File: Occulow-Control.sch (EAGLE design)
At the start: 39 parts, among them J1 CORTEX_DEBUG_PTH, T1 DMP3010LK3, T2 DMP3010LK3, T3 DMP3010LK3

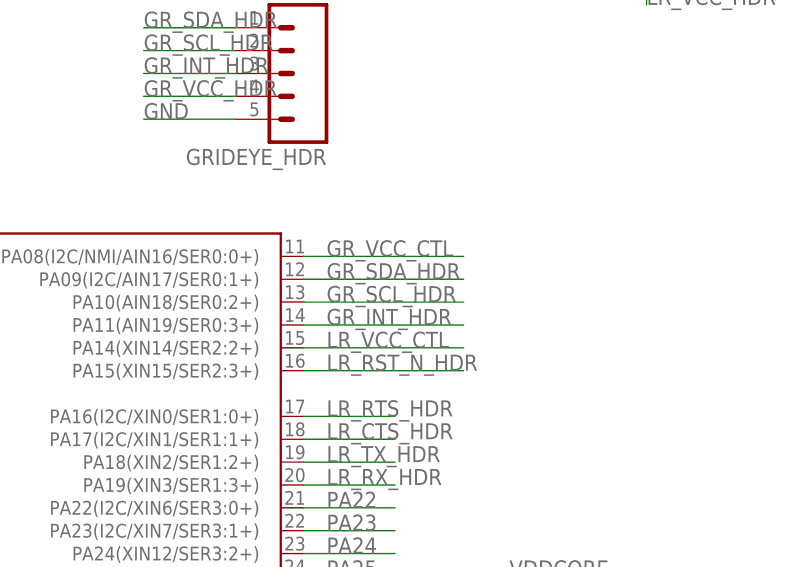
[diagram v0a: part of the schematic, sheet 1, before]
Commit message: Move schematic grideye pins to i2c pads, fixes #2
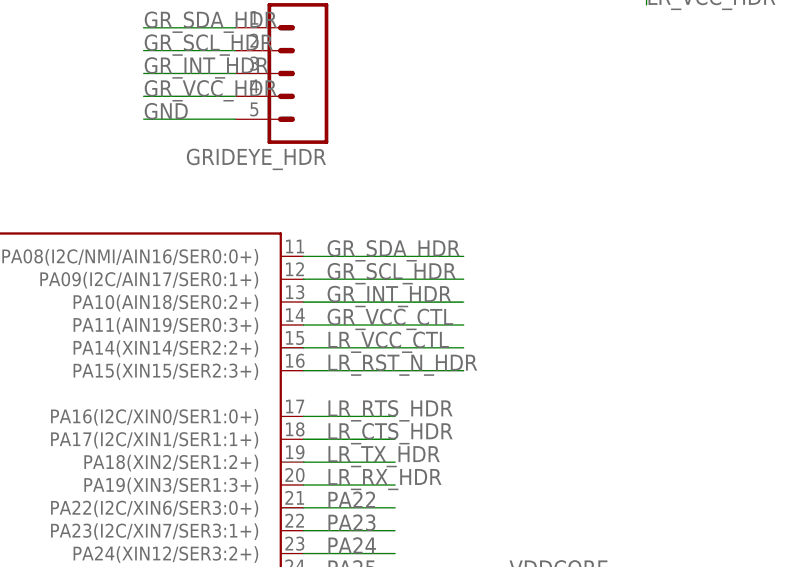
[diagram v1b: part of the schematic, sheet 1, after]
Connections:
- net GR_INT_HDR: now also U$1.PA10(AIN18/SER0:2+); no longer U$1.PA11(AIN19/SER0:3+)
- net GR_SCL_HDR: now also U$1.PA09(I2C/AIN17/SER0:1+); no longer U$1.PA10(AIN18/SER0:2+)
- net GR_SDA_HDR: now also U$1.PA08(I2C/NMI/AIN16/SER0:0+); no longer U$1.PA09(I2C/AIN17/SER0:1+)
- net GR_VCC_CTL: now also U$1.PA11(AIN19/SER0:3+); no longer U$1.PA08(I2C/NMI/AIN16/SER0:0+)
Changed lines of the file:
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@@
 </segment>
 <segment>
-<pinref part="U$1" gate="G$1" pin="PA09(I2C/AIN17/SER0:1+)"/>
-<wire x1="142.24" y1="93.98" x2="160.02" y2="93.98" width="0.1524" layer="91"/>
-<label x="144.78" y="93.98" size="1.778" layer="95"/>
+<pinref part="U$1" gate="G$1" pin="PA08(I2C/NMI/AIN16/SER0:0+)"/>
+<wire x1="142.24" y1="96.52" x2="160.02" y2="96.52" width="0.1524" layer="91"/>
+<label x="144.78" y="96.52" size="1.778" layer="95"/>
 </segment>
 </net>
@@
 </segment>
 <segment>
-<pinref part="U$1" gate="G$1" pin="PA10(AIN18/SER0:2+)"/>
-<wire x1="142.24" y1="91.44" x2="160.02" y2="91.44" width="0.1524" layer="91"/>
-<label x="144.78" y="91.44" size="1.778" layer="95"/>
+<pinref part="U$1" gate="G$1" pin="PA09(I2C/AIN17/SER0:1+)"/>
+<wire x1="142.24" y1="93.98" x2="160.02" y2="93.98" width="0.1524" layer="91"/>
+<label x="144.78" y="93.98" size="1.778" layer="95"/>
 </segment>
 </net>
@@
 </segment>
 <segment>
-<pinref part="U$1" gate="G$1" pin="PA11(AIN19/SER0:3+)"/>
-<label x="144.78" y="88.9" size="1.778" layer="95"/>
-<wire x1="160.02" y1="88.9" x2="142.24" y2="88.9" width="0.1524" layer="91"/>
+<pinref part="U$1" gate="G$1" pin="PA10(AIN18/SER0:2+)"/>
+<wire x1="142.24" y1="91.44" x2="160.02" y2="91.44" width="0.1524" layer="91"/>
+<label x="144.78" y="91.44" size="1.778" layer="95"/>
 </segment>
 </net>
@@
 </segment>
 <segment>
-<pinref part="U$1" gate="G$1" pin="PA08(I2C/NMI/AIN16/SER0:0+)"/>
-<wire x1="142.24" y1="96.52" x2="160.02" y2="96.52" width="0.1524" layer="91"/>
-<label x="144.78" y="96.52" size="1.778" layer="95"/>
+<pinref part="U$1" gate="G$1" pin="PA11(AIN19/SER0:3+)"/>
+<label x="144.78" y="88.9" size="1.778" layer="95"/>
+<wire x1="160.02" y1="88.9" x2="142.24" y2="88.9" width="0.1524" layer="91"/>
 </segment>
 </net>

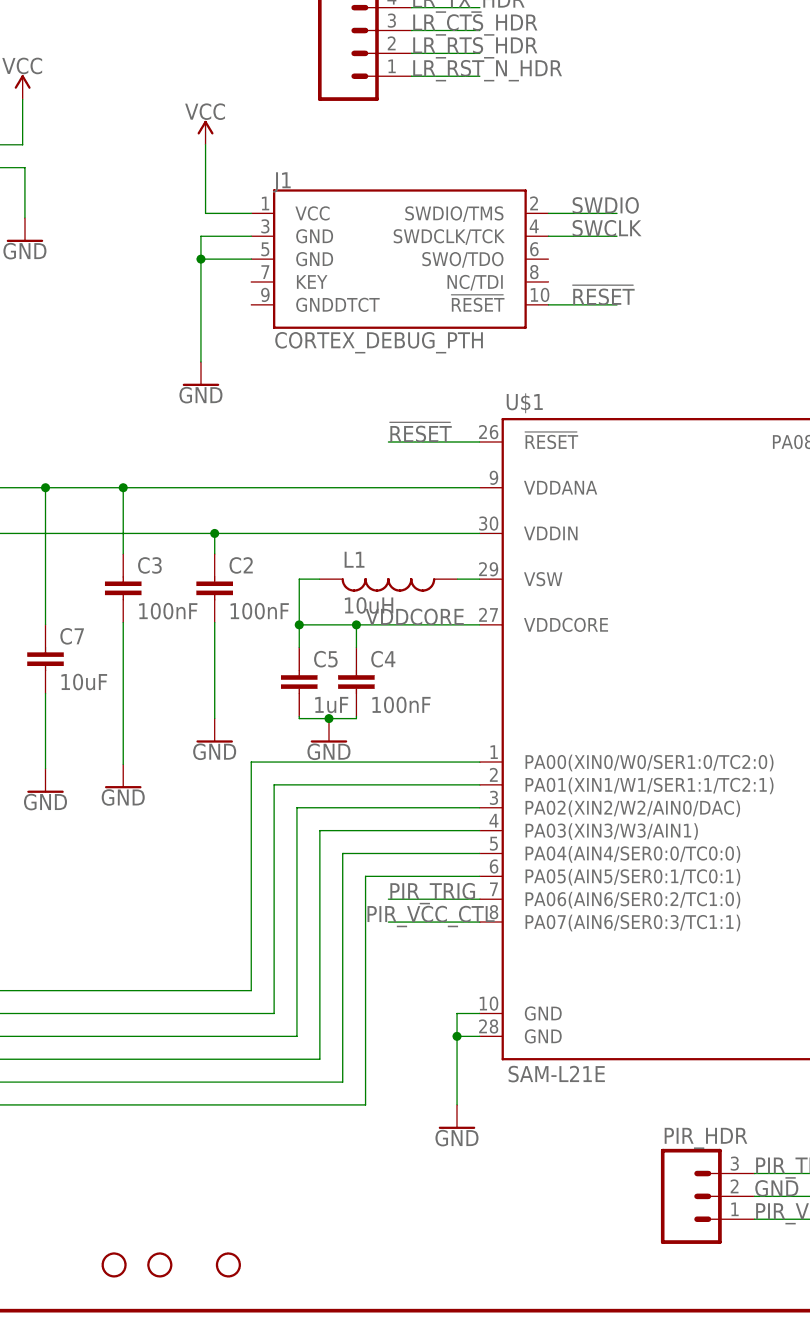
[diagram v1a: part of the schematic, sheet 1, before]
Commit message: Updated debug header, re-routed grideye header
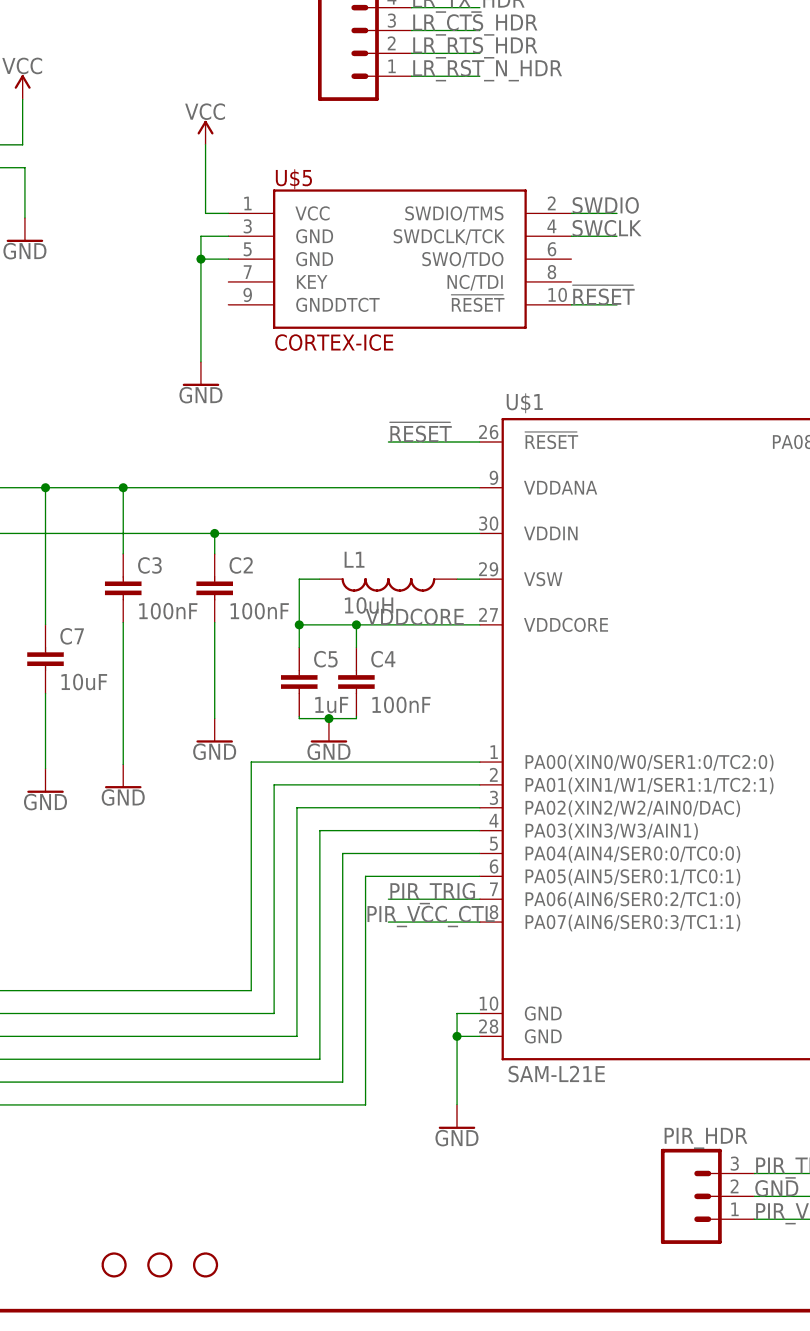
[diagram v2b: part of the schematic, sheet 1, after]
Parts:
- removed J1: CORTEX_DEBUG_PTH, SparkFun-Connectors:CORTEX_DEBUG_PTH
- added U$5: CORTEX-ICE, cortex-debug:CORTEX-ICE
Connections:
- net !RESET: now also U$5.!RESET; no longer J1.!RESET
- net GND: now also U$5.GND@3, U$5.GND@5; no longer J1.GND@3, J1.GND@5
- net SWCLK: now also U$5.SWDCLK/TCK; no longer J1.SWDCLK/TCK
- net SWDIO: now also U$5.SWDIO/TMS; no longer J1.SWDIO/TMS
- net VCC: now also U$5.VCC; no longer J1.VCC
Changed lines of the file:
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@@
 <part name="T3" library="transistor-fet" deviceset="SPD30P06P" device="TO252" value="DMP3010LK3"/>
 <part name="R1" library="resistor" deviceset="R-US_" device="R1206" value="1k"/>
-<part name="J1" library="SparkFun-Connectors" deviceset="CORTEX_DEBUG" device="_PTH"/>
 <part name="SUPPLY4" library="SparkFun-PowerSymbols" deviceset="VCC" device=""/>
 <part name="GND9" library="SparkFun-PowerSymbols" deviceset="GND" device=""/>
@@
 <part name="FRAME2" library="SparkFun-Aesthetics" deviceset="FRAME-LETTER" device="NO_PACKAGE"/>
 <part name="FRAME3" library="SparkFun-Aesthetics" deviceset="FRAME-LETTER" device="NO_PACKAGE"/>
+<part name="U$5" library="cortex-debug" deviceset="CORTEX-ICE" device=""/>
 </parts>
 <sheets>
@@
 <instance part="T3" gate="G$1" x="226.822" y="134.62"/>
 <instance part="R1" gate="G$1" x="165.1" y="53.34" rot="R90"/>
-<instance part="J1" gate="G$1" x="66.04" y="116.84"/>
 <instance part="SUPPLY4" gate="G$1" x="45.72" y="129.54"/>
 <instance part="GND9" gate="1" x="45.212" y="102.87"/>
@@
 <instance part="H1" gate="G$1" x="35.56" y="5.08"/>
 <instance part="H2" gate="G$1" x="40.64" y="5.08"/>
-<instance part="H3" gate="G$1" x="48.26" y="5.08"/>
+<instance part="H3" gate="G$1" x="45.72" y="5.08"/>
 <instance part="LR_CTL_HDR" gate="G$1" x="63.5" y="142.24"/>
+<instance part="U$5" gate="G$1" x="66.04" y="116.84"/>
 </instances>
 <busses>
@@
 </segment>
 <segment>
-<pinref part="J1" gate="G$1" pin="GND@3"/>
 <pinref part="GND9" gate="1" pin="GND"/>
-<wire x1="50.8" y1="119.38" x2="45.212" y2="119.38" width="0.1524" layer="91"/>
+<wire x1="48.26" y1="119.38" x2="45.212" y2="119.38" width="0.1524" layer="91"/>
 <wire x1="45.212" y1="119.38" x2="45.212" y2="116.84" width="0.1524" layer="91"/>
-<pinref part="J1" gate="G$1" pin="GND@5"/>
 <wire x1="45.212" y1="116.84" x2="45.212" y2="105.41" width="0.1524" layer="91"/>
-<wire x1="50.8" y1="116.84" x2="45.212" y2="116.84" width="0.1524" layer="91"/>
+<wire x1="48.26" y1="116.84" x2="45.212" y2="116.84" width="0.1524" layer="91"/>
 <junction x="45.212" y="116.84"/>
+<pinref part="U$5" gate="G$1" pin="GND@3"/>
+<pinref part="U$5" gate="G$1" pin="GND@5"/>
 </segment>
 <segment>
@@
 <net name="VCC" class="0">
 <segment>
-<pinref part="J1" gate="G$1" pin="VCC"/>
 <pinref part="SUPPLY4" gate="G$1" pin="VCC"/>
-<wire x1="50.8" y1="121.92" x2="45.72" y2="121.92" width="0.1524" layer="91"/>
+<wire x1="48.26" y1="121.92" x2="45.72" y2="121.92" width="0.1524" layer="91"/>
 <wire x1="45.72" y1="121.92" x2="45.72" y2="129.54" width="0.1524" layer="91"/>
+<pinref part="U$5" gate="G$1" pin="VCC"/>
 </segment>
 <segment>
@@
 </segment>
 <segment>
-<pinref part="J1" gate="G$1" pin="SWDCLK/TCK"/>
-<wire x1="83.82" y1="119.38" x2="91.44" y2="119.38" width="0.1524" layer="91"/>
+<wire x1="86.36" y1="119.38" x2="91.44" y2="119.38" width="0.1524" layer="91"/>
 <label x="86.36" y="119.38" size="1.778" layer="95"/>
+<pinref part="U$5" gate="G$1" pin="SWDCLK/TCK"/>
 </segment>
 </net>
@@
 <net name="SWDIO" class="0">
 <segment>
-<pinref part="J1" gate="G$1" pin="SWDIO/TMS"/>
-<wire x1="83.82" y1="121.92" x2="91.44" y2="121.92" width="0.1524" layer="91"/>
+<wire x1="86.36" y1="121.92" x2="91.44" y2="121.92" width="0.1524" layer="91"/>
 <label x="86.36" y="121.92" size="1.778" layer="95"/>
+<pinref part="U$5" gate="G$1" pin="SWDIO/TMS"/>
 </segment>
 <segment>
@@
 </segment>
 <segment>
-<pinref part="J1" gate="G$1" pin="!RESET"/>
-<wire x1="83.82" y1="111.76" x2="91.44" y2="111.76" width="0.1524" layer="91"/>
+<wire x1="86.36" y1="111.76" x2="91.44" y2="111.76" width="0.1524" layer="91"/>
 <label x="86.36" y="111.76" size="1.778" layer="95"/>
-</segment>
-</net>
+<pinref part="U$5" gate="G$1" pin="!RESET"/>
+</segment>
+</net>

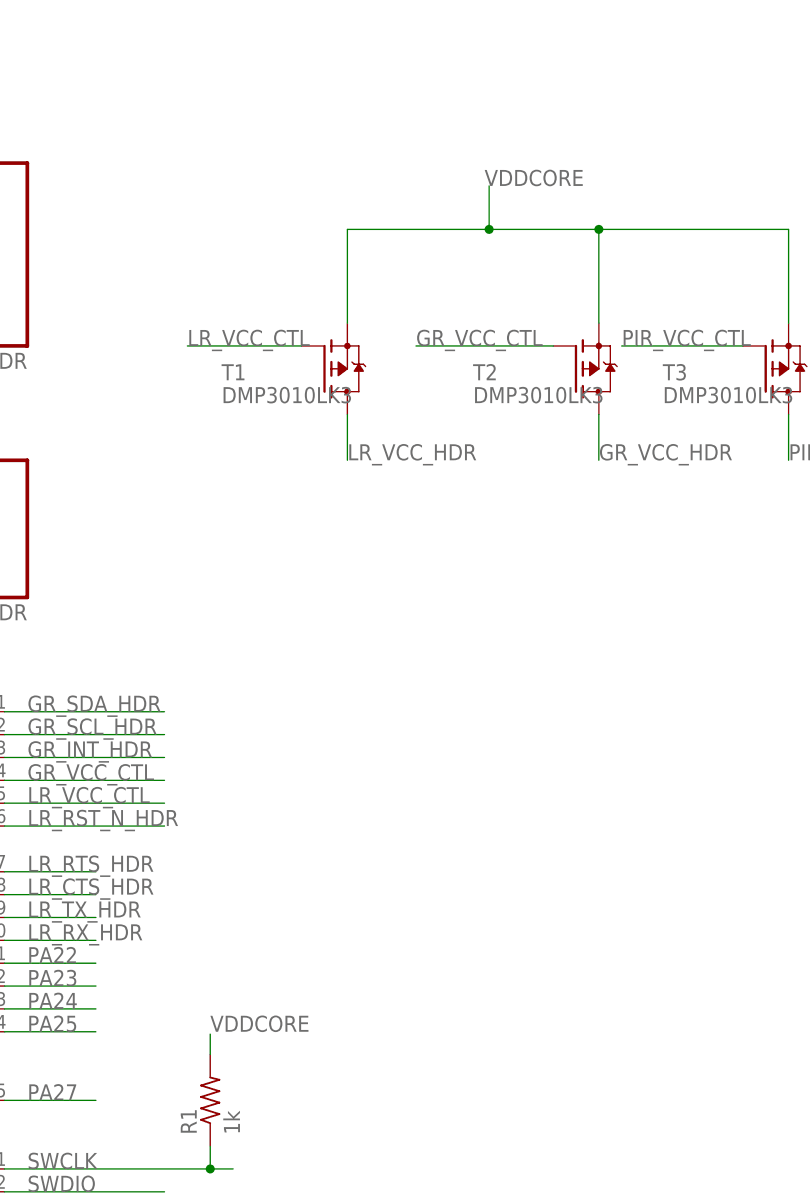
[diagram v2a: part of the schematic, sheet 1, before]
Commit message: No VDDCORE power, all vcc. Fixes #9
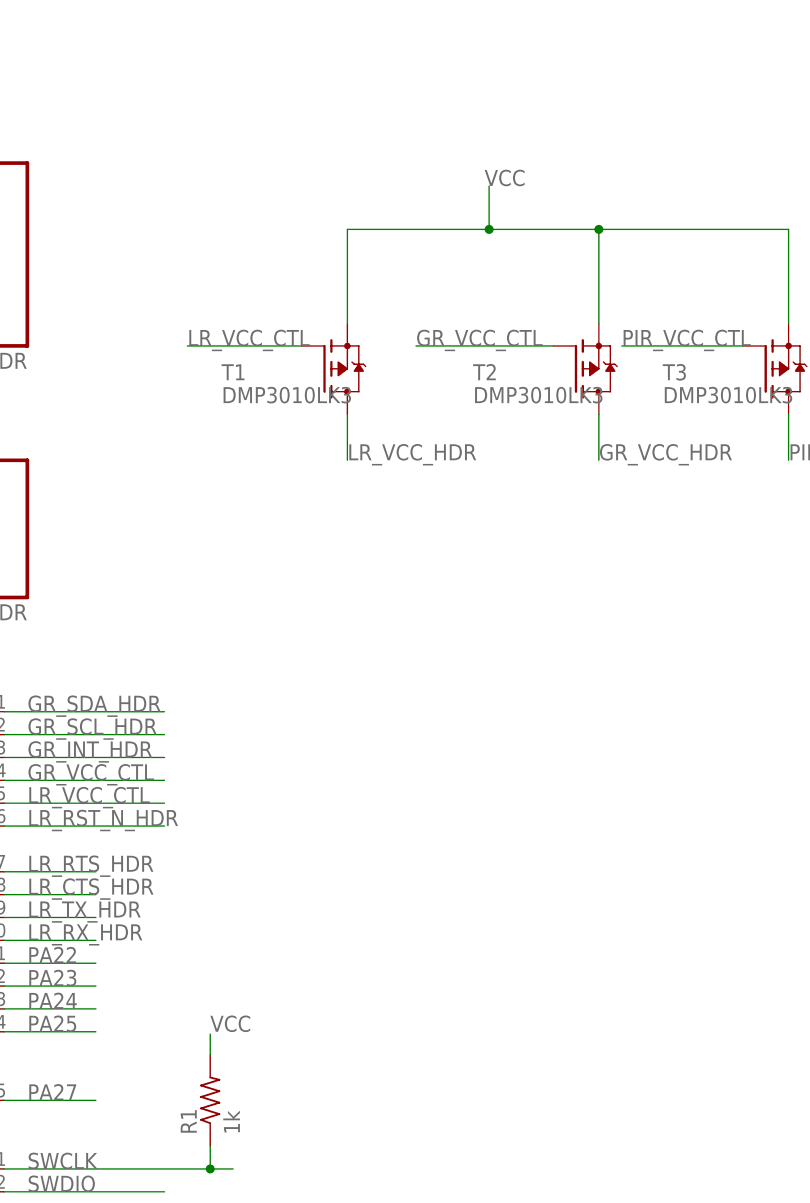
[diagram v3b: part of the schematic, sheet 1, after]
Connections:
- net VCC: now also R1.2, T1.S, T2.S, T3.S
- net VDDCORE: no longer R1.2, T1.S, T2.S, T3.S
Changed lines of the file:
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@@
 <wire x1="134.62" y1="142.24" x2="116.84" y2="142.24" width="0.1524" layer="91"/>
+</segment>
+<segment>
+<pinref part="R1" gate="G$1" pin="2"/>
+<wire x1="165.1" y1="60.706" x2="165.1" y2="58.42" width="0.1524" layer="91"/>
+<label x="165.1" y="60.96" size="1.778" layer="95"/>
+</segment>
+<segment>
+<wire x1="196.088" y1="154.94" x2="196.088" y2="150.114" width="0.1524" layer="91"/>
+<pinref part="T1" gate="G$1" pin="S"/>
+<wire x1="196.088" y1="150.114" x2="180.34" y2="150.114" width="0.1524" layer="91"/>
+<wire x1="180.34" y1="150.114" x2="180.34" y2="139.7" width="0.1524" layer="91"/>
+<pinref part="T2" gate="G$1" pin="S"/>
+<wire x1="196.088" y1="150.114" x2="208.28" y2="150.114" width="0.1524" layer="91"/>
+<wire x1="208.28" y1="150.114" x2="208.28" y2="139.7" width="0.1524" layer="91"/>
+<junction x="196.088" y="150.114"/>
+<pinref part="T3" gate="G$1" pin="S"/>
+<wire x1="208.28" y1="150.114" x2="229.362" y2="150.114" width="0.1524" layer="91"/>
+<wire x1="229.362" y1="150.114" x2="229.362" y2="139.7" width="0.1524" layer="91"/>
+<junction x="208.28" y="150.114"/>
+<label x="195.58" y="154.94" size="1.778" layer="95"/>
 </segment>
 </net>
@@
 <label x="63.5" y="76.2" size="1.778" layer="95"/>
 </segment>
-<segment>
-<wire x1="196.088" y1="154.94" x2="196.088" y2="150.114" width="0.1524" layer="91"/>
-<pinref part="T1" gate="G$1" pin="S"/>
-<wire x1="196.088" y1="150.114" x2="180.34" y2="150.114" width="0.1524" layer="91"/>
-<wire x1="180.34" y1="150.114" x2="180.34" y2="139.7" width="0.1524" layer="91"/>
-<pinref part="T2" gate="G$1" pin="S"/>
-<wire x1="196.088" y1="150.114" x2="208.28" y2="150.114" width="0.1524" layer="91"/>
-<wire x1="208.28" y1="150.114" x2="208.28" y2="139.7" width="0.1524" layer="91"/>
-<junction x="196.088" y="150.114"/>
-<pinref part="T3" gate="G$1" pin="S"/>
-<wire x1="208.28" y1="150.114" x2="229.362" y2="150.114" width="0.1524" layer="91"/>
-<wire x1="229.362" y1="150.114" x2="229.362" y2="139.7" width="0.1524" layer="91"/>
-<junction x="208.28" y="150.114"/>
-<label x="195.58" y="154.94" size="1.778" layer="95"/>
-</segment>
-<segment>
-<pinref part="R1" gate="G$1" pin="2"/>
-<wire x1="165.1" y1="60.706" x2="165.1" y2="58.42" width="0.1524" layer="91"/>
-<label x="165.1" y="60.96" size="1.778" layer="95"/>
-</segment>
-</net>
+</net>
